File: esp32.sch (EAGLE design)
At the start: 21 parts, among them IC1 LM1117IMPX-3.3, U1 ESP32MOD

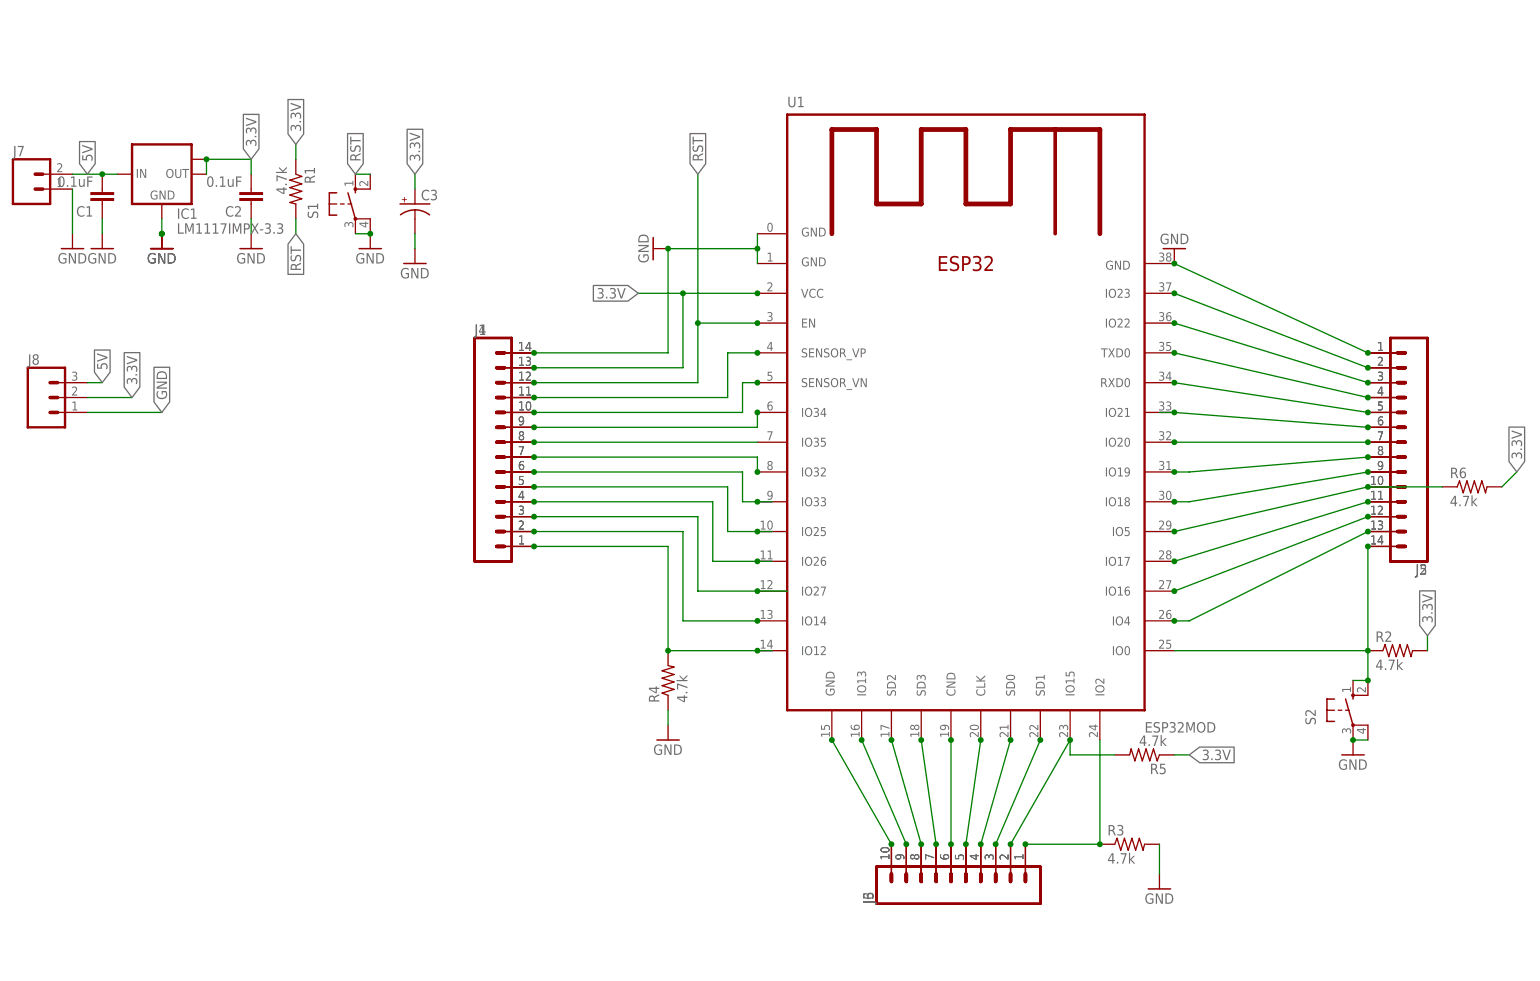
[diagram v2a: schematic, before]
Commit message: Added LEDs and improved reset circuitry
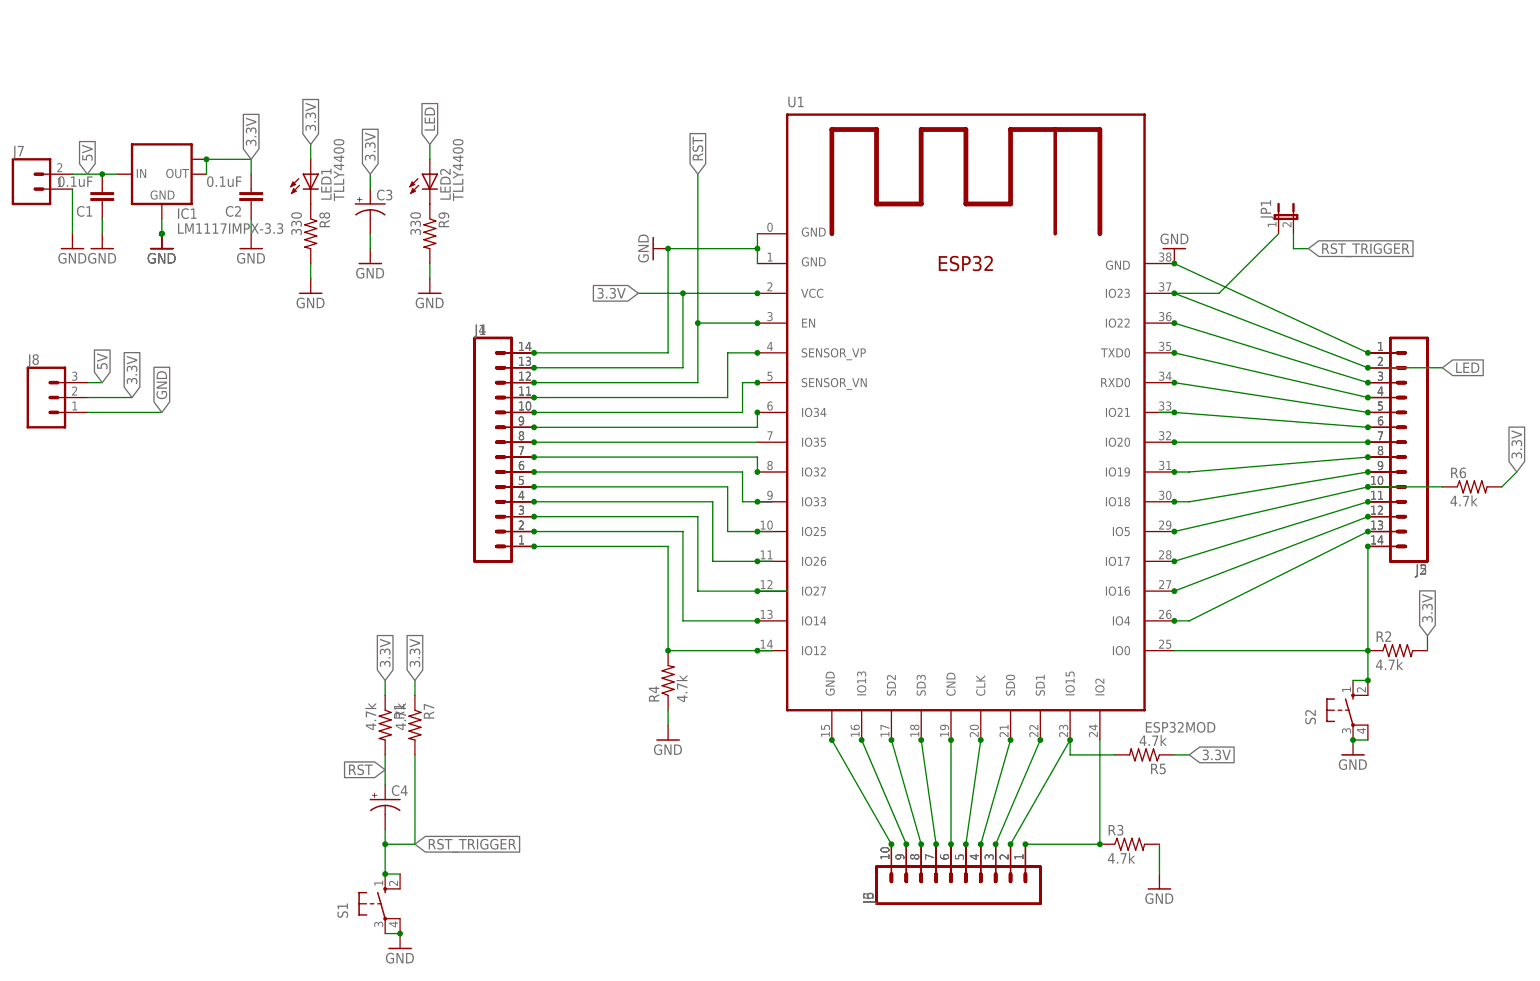
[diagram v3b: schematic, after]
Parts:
- added C4: (no value), rcl:CPOL-USE3.5-8
- added JP1: (no value), jumper:JP1E
- added LED1, LED2: TLLY4400, led:TLLY4400
- added R7: 4.7k, rcl:R-US_0411/15
- added R8, R9: 330, rcl:R-US_0411/15
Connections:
- removed net N$18: J2.2, J5.2, U1.IO23
- new net LED: J2.2, J5.2, JP1.1, LED2.A, U1.IO23
- new net N$4: LED1.C, R8.1
- new net N$5: LED2.C, R9.1
- new net RST_TRIGGER: C4.-, JP1.2, R7.2, S1.S, S1.S1
- net 3.3V: now also LED1.A, R7.1
- net GND: now also R8.2, R9.2
- net RST: now also C4.+; no longer S1.S, S1.S1
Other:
- moved on the sheet: C3, R1, S1

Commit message: Finalized the layout with cheap design
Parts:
- removed R2, R3, R4, R5, R6: 4.7k, rcl:R-US_0411/15
- removed U1: ESP32MOD, ESP3x:ESP32MOD
- added J10, J11: (no value), SparkFun-Connectors:CONN_14LONGPADS
- added J12: (no value), SparkFun-Connectors:CONN_10"
- added J9: (no value), SparkFun-Connectors:CONN_03
- added R10: 330, rcl:R-EU_0207/12
- added R11, R12, R13, R14: 4.7k, rcl:R-EU_0207/12
- R1, R7, R8: device rcl:R-US_0411/15 -> rcl:R-EU_0207/12
- R9: value 330 -> 4.7k; device rcl:R-US_0411/15 -> rcl:R-EU_0207/12
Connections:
- net 3.3V: now also J10.13, R11.2, R13.1, R14.1, R9.2; no longer R1.1, R2.2, R5.1, R6.2, U1.VCC
- net GND: now also J10.14, J11.1, J12.10, J9.1, R1.1, R10.1, R12.1, R8.1; no longer R3.2, R4.1, R8.2, R9.2, U1.GND, U1.GND@0, U1.GND@1, U1.GND@3
- net LED: now also J11.2; no longer U1.IO23
- net N$1: now also J11.7; no longer U1.IO20
- net N$10: now also J10.5; no longer U1.IO25
- net N$11: now also J10.4; no longer U1.IO26
- net N$12: now also J10.3; no longer U1.IO27
- net N$13: now also J10.2; no longer U1.IO14
- net N$14: now also J10.1, R1.2; no longer R4.2, U1.IO12
- net N$15: now also J11.5, J9.3; no longer U1.RXD0
- net N$16: now also J11.4, J9.2; no longer U1.TXD0
- net N$17: now also J11.3; no longer U1.IO22
- net N$19: now also J11.10, R14.2; no longer R6.1, U1.IO5
- net N$2: now also J10.11; no longer U1.SENSOR_VP
- net N$20: now also J11.6; no longer U1.IO21
- net N$22: now also J11.8; no longer U1.IO19
- net N$23: now also J11.9; no longer U1.IO18
- net N$25: now also J11.11; no longer U1.IO17
- net N$26: now also J11.12; no longer U1.IO16
- net N$27: now also J11.13; no longer U1.IO4
- net N$28: now also J11.14, R13.2; no longer R2.1, U1.IO0
- net N$3: now also J10.10; no longer U1.SENSOR_VN
- net N$30: now also J12.9; no longer U1.IO13
- net N$31: now also J12.8; no longer U1.SD2
- net N$32: now also J12.7; no longer U1.SD3
- net N$33: now also J12.6; no longer U1.CND
- net N$34: now also J12.5; no longer U1.CLK
- net N$35: now also J12.4; no longer U1.SD0
- net N$36: now also J12.3; no longer U1.SD1
- net N$37: now also J12.2, R7.2; no longer R5.2, U1.IO15
- net N$38: now also J12.1, R12.2; no longer R3.1, U1.IO2
- net N$4: now also R10.2; no longer R8.1
- net N$5: now also R8.2; no longer R9.1
- net N$6: now also J10.9; no longer U1.IO34
- net N$7: now also J10.8; no longer U1.IO35
- net N$8: now also J10.7; no longer U1.IO32
- net N$9: now also J10.6; no longer U1.IO33
- net RST: now also J10.12, R9.1; no longer R1.2, U1.EN
- net RST_TRIGGER: now also R11.1; no longer R7.2
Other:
- moved on the sheet: JP1
